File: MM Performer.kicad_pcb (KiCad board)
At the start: 4 copper layers, 74.8 x 84.8 mm, 44 parts, among them IC1 68000D, J1 VCC, J2 GND, J3 FPU Clock, U1 MC68030RC, U2 MC68881FN-SOC, U3 ATF16V8BJ, U4 ATF16V8BJ, U5 ATF16V8BJ, U6 ATF16V8BJ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

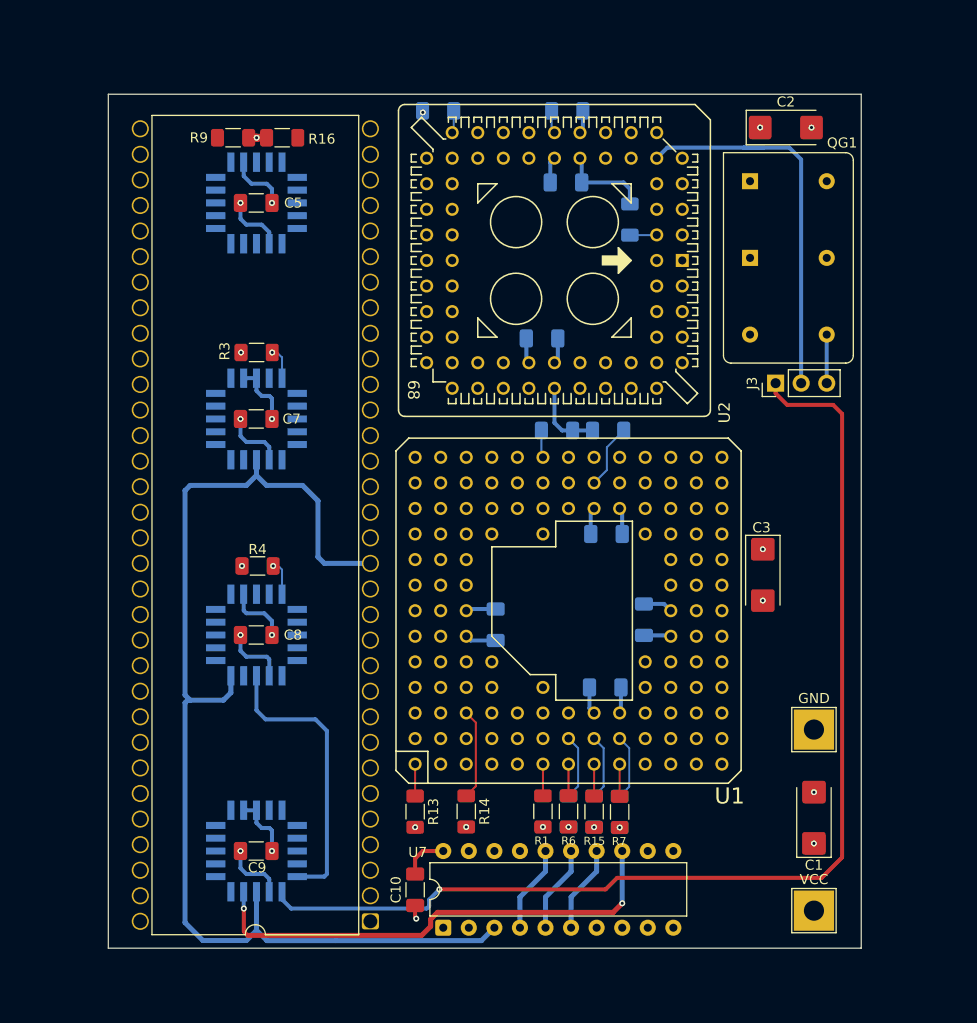
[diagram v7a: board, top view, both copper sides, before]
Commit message: Tweak the routing some more
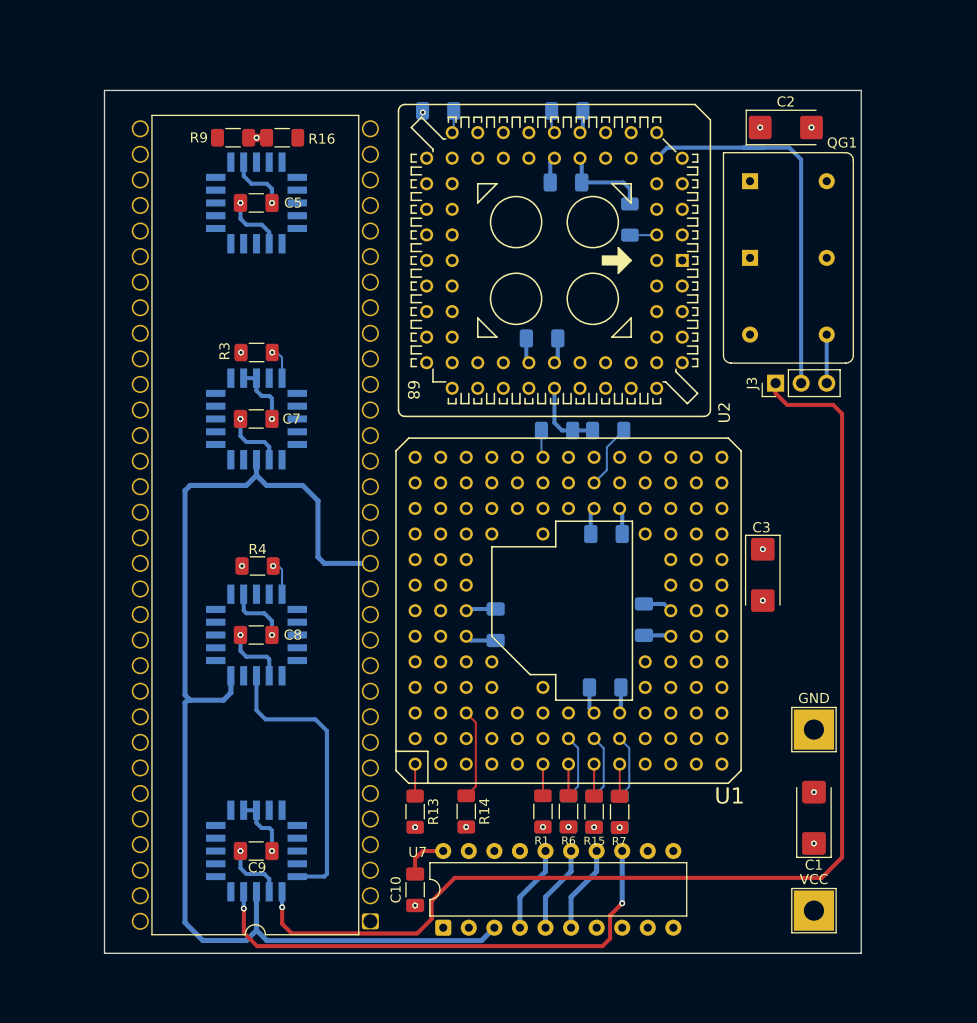
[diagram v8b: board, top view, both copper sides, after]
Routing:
- net /CLK_30: track 111.8 -> 115.9 mm
- net /C16M: track 48.6 -> 50.5 mm
- net GND: track 727.0 -> 728.1 mm
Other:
- board size 74.8 x 84.8 mm -> 75.2 x 85.7 mm
